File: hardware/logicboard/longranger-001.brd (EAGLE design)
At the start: 36 x 72 mm, 25 parts, among them IC1 74LS07N, IC2 LTC485N, IC3 LTC485N

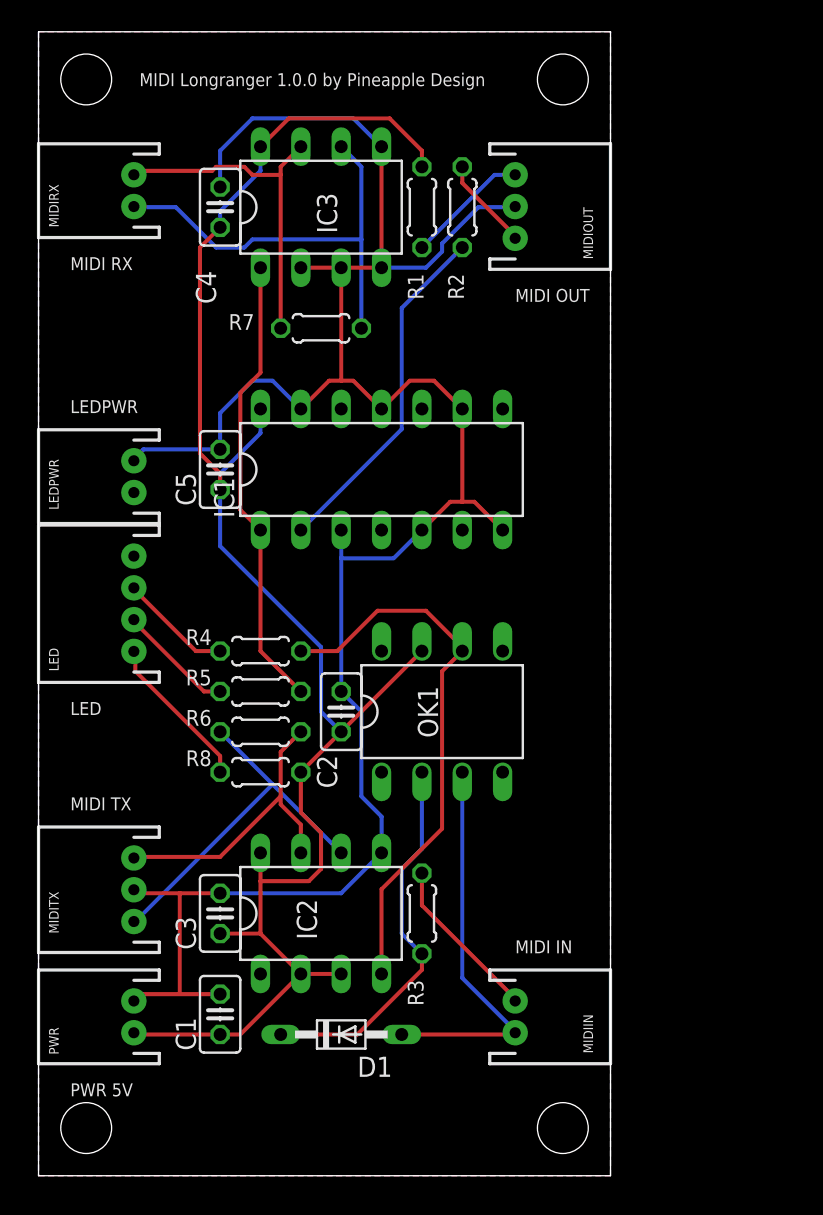
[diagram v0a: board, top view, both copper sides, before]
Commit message: New front panel.
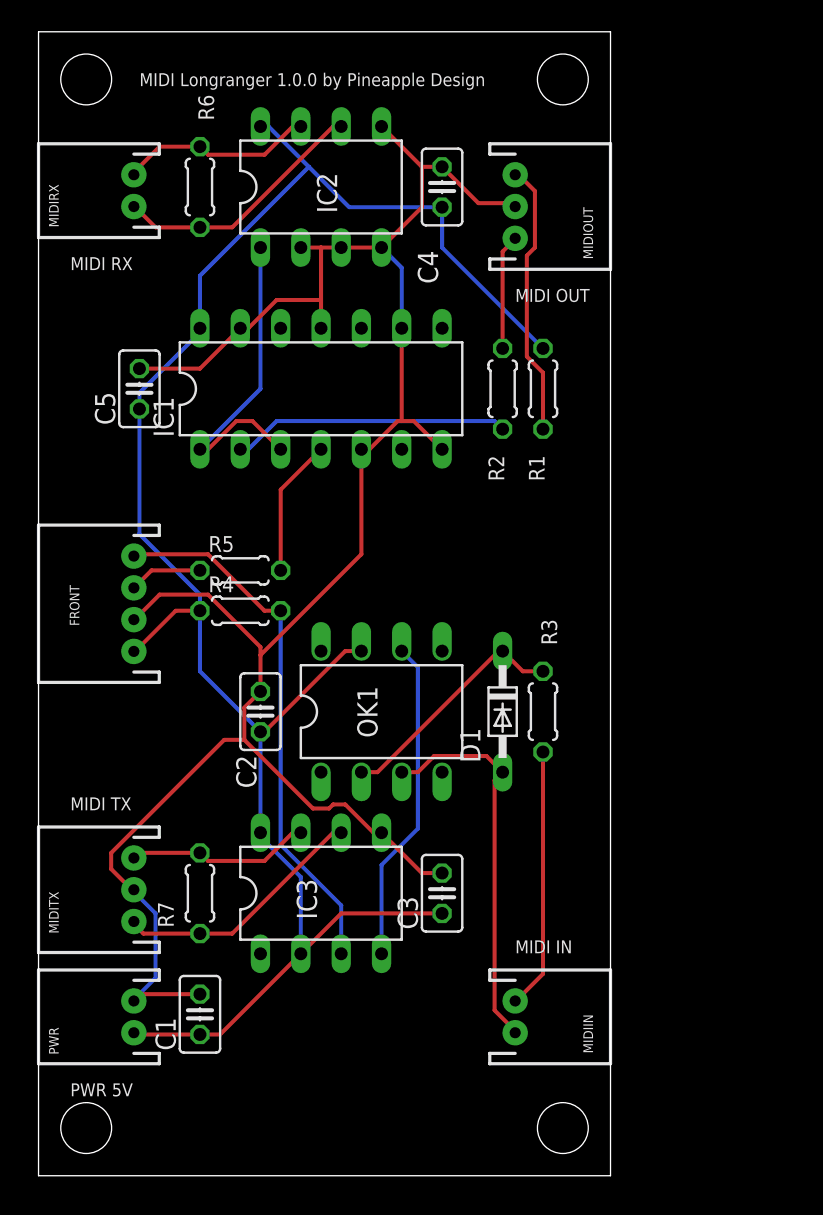
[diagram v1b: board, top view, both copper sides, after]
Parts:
- removed LEDPWR: (no value), SparkFun-Connectors:JST-2-PTH
- removed R8: 330, resistor:0204/5
- R4: value 330 -> 10k
- moved IC2 45.7 mm to (17.8, 62.2)
- moved IC3 43.2 mm to (17.8, 17.8)
- moved R7 36.4 mm to (10.2, 17.8), turned to 270 degrees
- moved R6 34.5 mm to (10.2, 62.2), turned to 270 degrees
- moved D1 22.7 mm to (29.2, 29.2), turned to 270 degrees
- moved R3 14.8 mm to (31.8, 29.2), turned to 270 degrees
- moved C3 14.0 mm to (25.4, 17.8)
- moved C4 14.0 mm to (25.4, 62.2)
- moved R1 13.7 mm to (31.8, 49.5)
- moved R2 11.7 mm to (29.2, 49.5)
- moved R5 7.73 mm to (12.7, 38.1), turned to 0 degrees
- moved C5 7.18 mm to (6.35, 49.5)
- moved IC1 6.35 mm to (17.8, 49.5)
- moved C2 5.08 mm to (14.0, 29.2)
- moved OK1 3.81 mm to (21.6, 29.2)
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- renumbered LED to FRONT
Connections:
- removed net N$5: FRONT.3, R4.2
- new net N$6: FRONT.4, IC3.3, R4.2
- net COM2: now also IC3.4; no longer IC2.4, R4.1
- net GND: now also FRONT.2, IC2.2, IC2.3, IC2.4; no longer IC1.3, IC3.2, IC3.3, IC3.4, LEDPWR.2
- net N$1: now also IC1.3, IC2.1; no longer IC3.1, R5.1
- net N$3: now also IC1.4, R5.2; no longer FRONT.1, R8.2
- net N$4: now also FRONT.3, R5.1; no longer FRONT.2, R5.2
- net RX+: now also IC2.6, R6.2; no longer IC3.6, R7.2
- net RX-: now also IC2.7, R6.1; no longer IC3.7, R7.1
- net TX+: now also IC3.6, R7.2; no longer IC2.6, R6.2
- net TX-: now also IC3.7, R7.1; no longer IC2.7, R6.1
- net VCC: now also FRONT.1, IC3.2, R4.1; no longer IC2.2, IC2.3, R8.1
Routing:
- net N$6: track 0.00 -> 33.9 mm
- net COM2: track 34.8 -> 20.4 mm
- net RX+: track 27.5 -> 16.2 mm
- net VCC: track 108.4 -> 119.5 mm
- net MIDITX+: track 7.76 -> 17.3 mm
- net RX-: track 21.7 -> 12.3 mm
- net N$15: track 24.1 -> 15.1 mm
- net N$1: track 28.8 -> 20.8 mm
- net TX-: track 19.5 -> 11.6 mm
- net GND: track 140.3 -> 132.8 mm
- net N$5: track 7.11 -> 0.00 mm
- net TX+: track 23.1 -> 16.1 mm
- net MIDIRX+: track 10.5 -> 16.4 mm
- net N$2: track 22.0 -> 17.5 mm
- net N$4: track 7.35 -> 4.61 mm
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- removed copper zone on layer 1, net GND
- removed copper zone on layer 16, net GND
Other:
- board text removed: "LED"
- board text removed: "LEDPWR"

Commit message: Ultra slim logicboard. Needs to refine silk pattern.
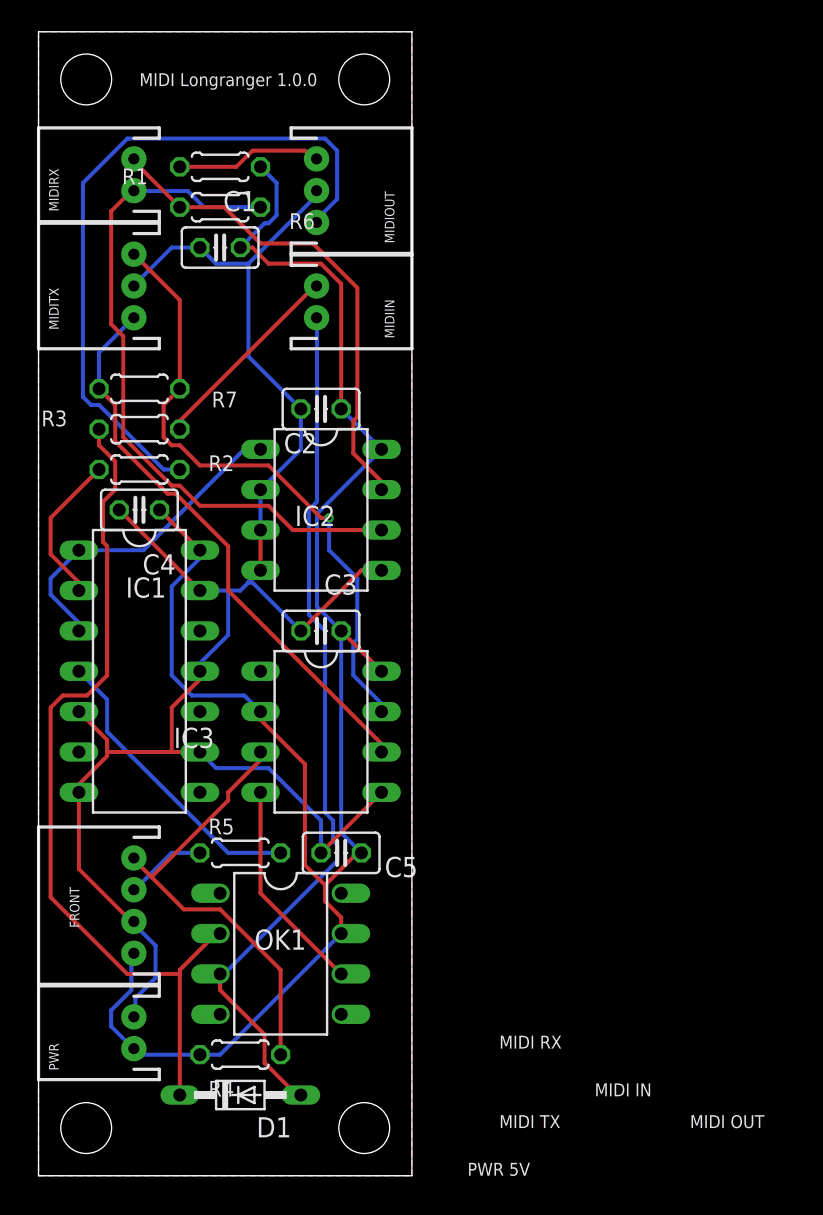
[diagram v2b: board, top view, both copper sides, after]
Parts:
- moved C1 48.3 mm to (11.4, 58.4), turned to 180 degrees
- moved MIDIIN 46.7 mm to (17.5, 55.0)
- moved MIDITX 38.0 mm to (6.00, 56.0)
- moved R7 32.0 mm to (6.35, 49.5), turned to 180 degrees
- moved C5 31.9 mm to (19.1, 20.3), turned to 180 degrees
- moved R3 31.0 mm to (6.35, 47.0), turned to 0 degrees
- moved D1 29.2 mm to (12.7, 5.08), turned to 0 degrees
- moved R4 27.9 mm to (12.7, 7.62)
- moved C4 27.9 mm to (6.35, 41.9), turned to 180 degrees
- moved R1 24.7 mm to (11.4, 63.5), turned to 0 degrees
- moved R2 23.4 mm to (6.35, 44.5), turned to 0 degrees
- moved IC1 21.1 mm to (6.35, 31.8), turned to 270 degrees
- moved IC2 20.3 mm to (17.8, 41.9), turned to 270 degrees
- moved C2 19.4 mm to (17.8, 48.3), turned to 180 degrees
- moved FRONT 19.0 mm to (6.00, 17.0)
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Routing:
- net N$15: track 15.1 -> 54.2 mm
- net MIDITX-: track 7.25 -> 44.0 mm
- net MIDIRX-: track 24.3 -> 55.3 mm
- net TX-: track 11.6 -> 39.4 mm, vias 0 -> 1
- net RX+: track 16.2 -> 43.6 mm
- net TX+: track 16.1 -> 35.9 mm
- net RX-: track 12.3 -> 31.0 mm
- net GND: track 132.8 -> 117.2 mm
- net N$3: track 8.67 -> 18.6 mm
- net MIDITX+: track 17.3 -> 9.24 mm
- net N$2: track 17.5 -> 9.62 mm
- net COM2: track 20.4 -> 13.5 mm
- net N$6: track 33.9 -> 28.2 mm
- net MIDIRX+: track 16.4 -> 12.6 mm
- net VCC: track 119.5 -> 118.8 mm
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- added copper zone on layer 1, net GND
- added copper zone on layer 16, net GND
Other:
- board size 36 x 72 mm -> 23.5 x 72 mm
- board text added: "MIDI Longranger 1.0.0"
- board text removed: "MIDI Longranger 1.0.0 by Pineapple Design"
